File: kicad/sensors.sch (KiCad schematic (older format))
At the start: 13 parts, among them J6 Proximity sensor, U5 KTIR0711S, U7 KTIR0711S, U8 KTIR0711S, U9 KTIR0711S

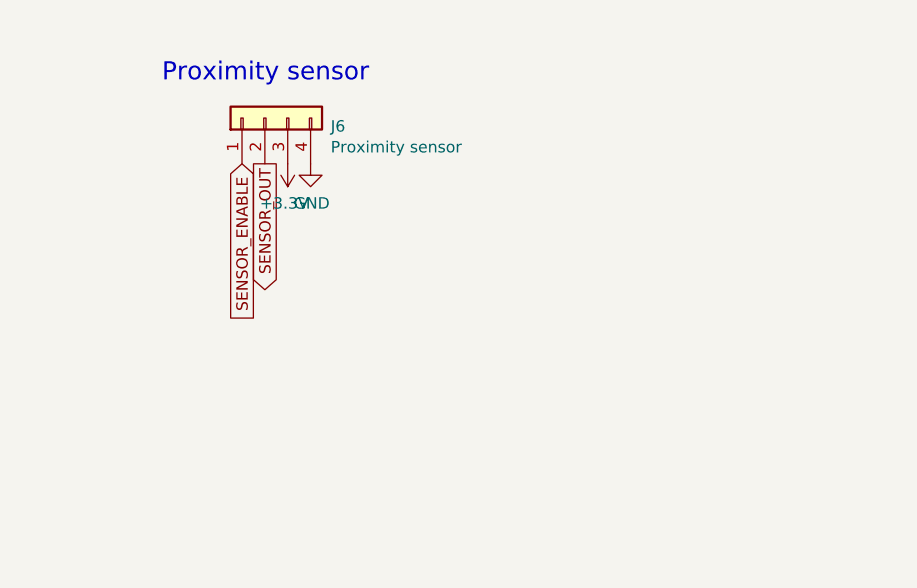
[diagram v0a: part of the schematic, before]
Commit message: fixed diodes, h bridge and modified power supply
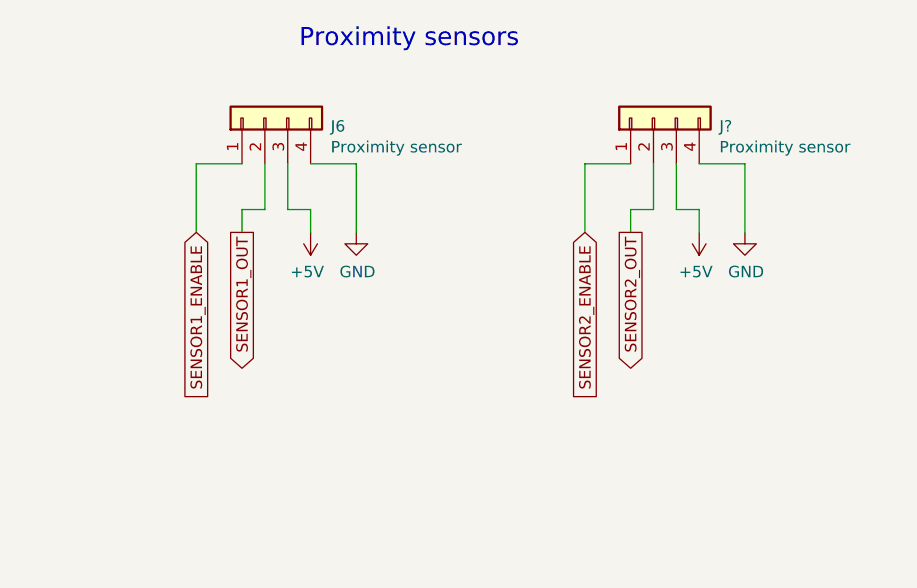
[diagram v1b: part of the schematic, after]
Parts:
- added J?: Proximity sensor, symbol Connector_Generic:Conn_01x04
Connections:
- net +3V3 is gone; now on net +5V: J6.3 (Pin_3)
- net +5V: now also J?.3 (Pin_3)
- net GND: now also J?.4 (Pin_4)
- net SENSOR_ENABLE renamed SENSOR1_ENABLE
- net SENSOR_OUT renamed SENSOR1_OUT
- new net SENSOR2_ENABLE: J?.1 (Pin_1)
- new net SENSOR2_OUT: J?.2 (Pin_2)
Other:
- note added: "Proximity sensors"
- note removed: "Proximity sensor"
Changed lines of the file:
@@
 KTIR_2
-$Comp
-L roboty_mobilne-rescue:KTIR0711S-warsztaty U?
-U 1 1 60BA4003
-P 2150 2350
-AR Path="/60BA4003" Ref="U?"  Part="1"
-AR Path="/60B6A5B0/60BA4003" Ref="U5"  Part="1"
-F 0 "U5" H 2150 2675 50  0000 C CNN
-F 1 "KTIR0711S" H 2150 2584 50  0000 C CNN
-F 2 "" H 1950 2150 50  0000 L CIN
-F 3 "" H 2150 2350 50  0000 L CNN
-	1    2150 2350
-	1    0    0    -1
-$EndComp
 $Comp
 L power:GND #PWR?
@@
 Wire Wire Line
 	1850 2600 2150 2600
-Wire Wire Line
-	2450 2450 2450 2600
-Wire Wire Line
-	2450 2600 2150 2600
-Connection ~ 2150 2600
 $Comp
 L Device:R_Small R?
@@
 	1    0    0    -1
 $EndComp
-$Comp
-L Device:R_Small R?
-U 1 1 60BA401A
-P 2550 2100
-AR Path="/60BA401A" Ref="R?"  Part="1"
-AR Path="/60B6A5B0/60BA401A" Ref="R7"  Part="1"
-F 0 "R7" H 2609 2146 50  0000 L CNN
-F 1 "10k" H 2609 2055 50  0000 L CNN
-F 2 "" V 2480 2100 50  0001 C CNN
-F 3 "~" H 2550 2100 50  0001 C CNN
-	1    2550 2100
-	1    0    0    -1
-$EndComp
 Wire Wire Line
 	1850 2250 1750 2250
-Text GLabel 2700 2250 2    50   Output ~ 0
-KTIR_1
 Text Notes 1650 1600 0    79   ~ 0
 White line sensors
@@
 	1    0    0    -1
 $EndComp
-Connection ~ 2150 1950
-Wire Wire Line
-	2150 1950 2550 1950
 Wire Wire Line
 	1750 3100 2150 3100
@@
 	1750 1950 1750 2000
 Wire Wire Line
-	2450 2250 2550 2250
-Wire Wire Line
 	1750 2200 1750 2250
-Wire Wire Line
-	2550 2200 2550 2250
-Connection ~ 2550 2250
-Wire Wire Line
-	2550 2250 2700 2250
-Wire Wire Line
-	2550 2000 2550 1950
 Wire Wire Line
 	1750 3100 1750 3150
@@
 Wire Wire Line
 	1750 4350 1750 4300
-Text Notes 3900 1600 0    79   ~ 0
-Proximity sensor
+Text Notes 4500 1450 0    79   ~ 0
+Proximity sensors
+$Comp
+L power:+5V #PWR0144
+U 1 1 60AEE18F
+P 2150 3100
+F 0 "#PWR0144" H 2150 2950 50  0001 C CNN
+F 1 "+5V" H 2165 3273 50  0000 C CNN
+F 2 "" H 2150 3100 50  0001 C CNN
+F 3 "" H 2150 3100 50  0001 C CNN
+	1    2150 3100
+	1    0    0    -1
+$EndComp
+Connection ~ 2150 3100
+Wire Wire Line
+	2150 3100 2550 3100
+Connection ~ 2150 1950
+Connection ~ 2150 2600
+Wire Wire Line
+	4050 1950 4050 2250
+Wire Wire Line
+	4250 1950 4050 1950
+Wire Wire Line
+	4750 1950 4750 2250
+Wire Wire Line
+	4550 1950 4750 1950
+$Comp
+L power:+5V #PWR?
+U 1 1 60BD6E0F
+P 4550 2250
+F 0 "#PWR?" H 4550 2100 50  0001 C CNN
+F 1 "+5V" H 4565 2423 50  0000 C CNN
+F 2 "" H 4550 2250 50  0001 C CNN
+F 3 "" H 4550 2250 50  0001 C CNN
+	1    4550 2250
+	-1   0    0    1
+$EndComp
+Text GLabel 4050 2250 3    50   Input ~ 0
+SENSOR1_ENABLE
+Text GLabel 4250 2250 3    50   Output ~ 0
+SENSOR1_OUT
+$Comp
+L power:GND #PWR?
+U 1 1 60BAA02E
+P 4750 2250
+AR Path="/60BAA02E" Ref="#PWR?"  Part="1"
+AR Path="/60B6A5B0/60BAA02E" Ref="#PWR0142"  Part="1"
+F 0 "#PWR0142" H 4750 2000 50  0001 C CNN
+F 1 "GND" H 4755 2077 50  0000 C CNN
+F 2 "" H 4750 2250 50  0001 C CNN
+F 3 "" H 4750 2250 50  0001 C CNN
+	1    4750 2250
+	1    0    0    -1
+$EndComp
 $Comp
 L Connector_Generic:Conn_01x04 J?
@@
 	0    -1   -1   0
 $EndComp
+Wire Wire Line
+	2550 2000 2550 1950
+Wire Wire Line
+	2550 2250 2700 2250
+Connection ~ 2550 2250
+Wire Wire Line
+	2550 2200 2550 2250
+Wire Wire Line
+	2450 2250 2550 2250
+Wire Wire Line
+	2150 1950 2550 1950
+Text GLabel 2700 2250 2    50   Output ~ 0
+KTIR_1
+$Comp
+L Device:R_Small R?
+U 1 1 60BA401A
+P 2550 2100
+AR Path="/60BA401A" Ref="R?"  Part="1"
+AR Path="/60B6A5B0/60BA401A" Ref="R7"  Part="1"
+F 0 "R7" H 2609 2146 50  0000 L CNN
+F 1 "10k" H 2609 2055 50  0000 L CNN
+F 2 "" V 2480 2100 50  0001 C CNN
+F 3 "~" H 2550 2100 50  0001 C CNN
+	1    2550 2100
+	1    0    0    -1
+$EndComp
+Wire Wire Line
+	2450 2600 2150 2600
+Wire Wire Line
+	2450 2450 2450 2600
+$Comp
+L roboty_mobilne-rescue:KTIR0711S-warsztaty U?
+U 1 1 60BA4003
+P 2150 2350
+AR Path="/60BA4003" Ref="U?"  Part="1"
+AR Path="/60B6A5B0/60BA4003" Ref="U5"  Part="1"
+F 0 "U5" H 2150 2675 50  0000 C CNN
+F 1 "KTIR0711S" H 2150 2584 50  0000 C CNN
+F 2 "" H 1950 2150 50  0000 L CIN
+F 3 "" H 2150 2350 50  0000 L CNN
+	1    2150 2350
+	1    0    0    -1
+$EndComp
+Wire Wire Line
+	4250 2250 4250 2150
+Wire Wire Line
+	4250 2150 4350 2150
+Wire Wire Line
+	4350 2150 4350 1950
+Wire Wire Line
+	4550 2250 4550 2150
+Wire Wire Line
+	4550 2150 4450 2150
+Wire Wire Line
+	4450 2150 4450 1950
+Wire Wire Line
+	5750 1950 5750 2250
+Wire Wire Line
+	5950 1950 5750 1950
+Wire Wire Line
+	6450 1950 6450 2250
+Wire Wire Line
+	6250 1950 6450 1950
+$Comp
+L power:+5V #PWR?
+U 1 1 60C05462
+P 6250 2250
+F 0 "#PWR?" H 6250 2100 50  0001 C CNN
+F 1 "+5V" H 6265 2423 50  0000 C CNN
+F 2 "" H 6250 2250 50  0001 C CNN
+F 3 "" H 6250 2250 50  0001 C CNN
+	1    6250 2250
+	-1   0    0    1
+$EndComp
+Text GLabel 5750 2250 3    50   Input ~ 0
+SENSOR2_ENABLE
+Text GLabel 5950 2250 3    50   Output ~ 0
+SENSOR2_OUT
 $Comp
 L power:GND #PWR?
-U 1 1 60BAA02E
-P 4550 1950
-AR Path="/60BAA02E" Ref="#PWR?"  Part="1"
-AR Path="/60B6A5B0/60BAA02E" Ref="#PWR0142"  Part="1"
-F 0 "#PWR0142" H 4550 1700 50  0001 C CNN
-F 1 "GND" H 4555 1777 50  0000 C CNN
-F 2 "" H 4550 1950 50  0001 C CNN
-F 3 "" H 4550 1950 50  0001 C CNN
-	1    4550 1950
-	1    0    0    -1
-$EndComp
-$Comp
-L power:+3.3V #PWR?
-U 1 1 60BAA034
-P 4450 1950
-AR Path="/60BAA034" Ref="#PWR?"  Part="1"
-AR Path="/60B6A5B0/60BAA034" Ref="#PWR0143"  Part="1"
-F 0 "#PWR0143" H 4450 1800 50  0001 C CNN
-F 1 "+3.3V" H 4465 2123 50  0000 C CNN
-F 2 "" H 4450 1950 50  0001 C CNN
-F 3 "" H 4450 1950 50  0001 C CNN
-	1    4450 1950
-	-1   0    0    1
-$EndComp
-Text GLabel 4350 1950 3    50   Output ~ 0
-SENSOR_OUT
-Text GLabel 4250 1950 3    50   Input ~ 0
-SENSOR_ENABLE
-$Comp
-L power:+5V #PWR0144
-U 1 1 60AEE18F
-P 2150 3100
-F 0 "#PWR0144" H 2150 2950 50  0001 C CNN
-F 1 "+5V" H 2165 3273 50  0000 C CNN
-F 2 "" H 2150 3100 50  0001 C CNN
-F 3 "" H 2150 3100 50  0001 C CNN
-	1    2150 3100
-	1    0    0    -1
-$EndComp
-Connection ~ 2150 3100
-Wire Wire Line
-	2150 3100 2550 3100
+U 1 1 60C0546A
+P 6450 2250
+AR Path="/60C0546A" Ref="#PWR?"  Part="1"
+AR Path="/60B6A5B0/60C0546A" Ref="#PWR?"  Part="1"
+F 0 "#PWR?" H 6450 2000 50  0001 C CNN
+F 1 "GND" H 6455 2077 50  0000 C CNN
+F 2 "" H 6450 2250 50  0001 C CNN
+F 3 "" H 6450 2250 50  0001 C CNN
+	1    6450 2250
+	1    0    0    -1
+$EndComp
+$Comp
+L Connector_Generic:Conn_01x04 J?
+U 1 1 60C05470
+P 6050 1750
+AR Path="/60C05470" Ref="J?"  Part="1"
+AR Path="/60B6A5B0/60C05470" Ref="J?"  Part="1"
+F 0 "J?" V 6014 1462 50  0000 R CNN
+F 1 "Proximity sensor" V 5923 1462 50  0000 R CNN
+F 2 "" H 6050 1750 50  0001 C CNN
+F 3 "~" H 6050 1750 50  0001 C CNN
+	1    6050 1750
+	0    -1   -1   0
+$EndComp
+Wire Wire Line
+	5950 2250 5950 2150
+Wire Wire Line
+	5950 2150 6050 2150
+Wire Wire Line
+	6050 2150 6050 1950
+Wire Wire Line
+	6250 2250 6250 2150
+Wire Wire Line
+	6250 2150 6150 2150
+Wire Wire Line
+	6150 2150 6150 1950
 $EndSCHEMATC

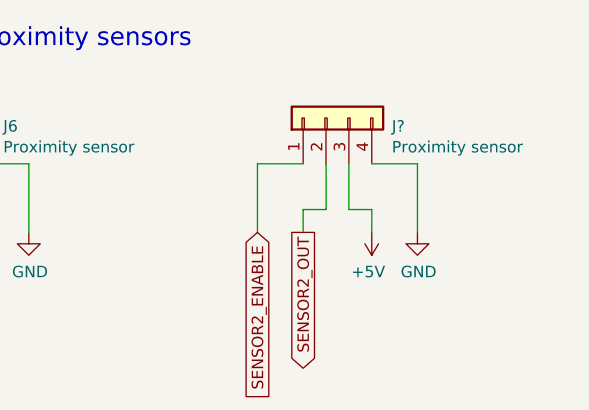
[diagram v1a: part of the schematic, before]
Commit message: deleted 3.3V and modified everything to use 5V instead
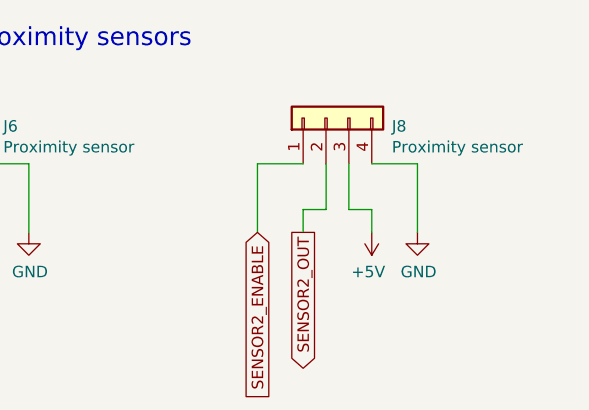
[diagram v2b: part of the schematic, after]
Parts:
- J6: footprint (none) -> Connector_PinSocket_2.54mm:PinSocket_1x04_P2.54mm_Vertical
- J8: renamed from J?; footprint (none) -> Connector_PinSocket_2.54mm:PinSocket_1x04_P2.54mm_Vertical
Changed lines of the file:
@@
 F 0 "U9" H 2150 6225 50  0000 C CNN
 F 1 "KTIR0711S" H 2150 6134 50  0000 C CNN
-F 2 "" H 1950 5700 50  0000 L CIN
+F 2 "" H 1950 5700 50  0001 L CIN
 F 3 "" H 2150 5900 50  0000 L CNN
 	1    2150 5900
@@
 F 0 "U7" H 2150 3825 50  0000 C CNN
 F 1 "KTIR0711S" H 2150 3734 50  0000 C CNN
-F 2 "" H 1950 3300 50  0000 L CIN
+F 2 "" H 1950 3300 50  0001 L CIN
 F 3 "" H 2150 3500 50  0000 L CNN
 	1    2150 3500
@@
 F 0 "U8" H 2150 5025 50  0000 C CNN
 F 1 "KTIR0711S" H 2150 4934 50  0000 C CNN
-F 2 "" H 1950 4500 50  0000 L CIN
+F 2 "" H 1950 4500 50  0001 L CIN
 F 3 "" H 2150 4700 50  0000 L CNN
 	1    2150 4700
@@
 	4550 1950 4750 1950
 $Comp
-L power:+5V #PWR?
+L power:+5V #PWR0145
 U 1 1 60BD6E0F
 P 4550 2250
-F 0 "#PWR?" H 4550 2100 50  0001 C CNN
+F 0 "#PWR0145" H 4550 2100 50  0001 C CNN
 F 1 "+5V" H 4565 2423 50  0000 C CNN
 F 2 "" H 4550 2250 50  0001 C CNN
@@
 F 0 "J6" V 4314 1462 50  0000 R CNN
 F 1 "Proximity sensor" V 4223 1462 50  0000 R CNN
-F 2 "" H 4350 1750 50  0001 C CNN
+F 2 "Connector_PinSocket_2.54mm:PinSocket_1x04_P2.54mm_Vertical" H 4350 1750 50  0001 C CNN
 F 3 "~" H 4350 1750 50  0001 C CNN
 	1    4350 1750
@@
 F 0 "U5" H 2150 2675 50  0000 C CNN
 F 1 "KTIR0711S" H 2150 2584 50  0000 C CNN
-F 2 "" H 1950 2150 50  0000 L CIN
+F 2 "" H 1950 2150 50  0001 L CIN
 F 3 "" H 2150 2350 50  0000 L CNN
 	1    2150 2350
@@
 	6250 1950 6450 1950
 $Comp
-L power:+5V #PWR?
+L power:+5V #PWR0146
 U 1 1 60C05462
 P 6250 2250
-F 0 "#PWR?" H 6250 2100 50  0001 C CNN
+F 0 "#PWR0146" H 6250 2100 50  0001 C CNN
 F 1 "+5V" H 6265 2423 50  0000 C CNN
 F 2 "" H 6250 2250 50  0001 C CNN
@@
 P 6450 2250
 AR Path="/60C0546A" Ref="#PWR?"  Part="1"
-AR Path="/60B6A5B0/60C0546A" Ref="#PWR?"  Part="1"
-F 0 "#PWR?" H 6450 2000 50  0001 C CNN
+AR Path="/60B6A5B0/60C0546A" Ref="#PWR0147"  Part="1"
+F 0 "#PWR0147" H 6450 2000 50  0001 C CNN
 F 1 "GND" H 6455 2077 50  0000 C CNN
 F 2 "" H 6450 2250 50  0001 C CNN
@@
 P 6050 1750
 AR Path="/60C05470" Ref="J?"  Part="1"
-AR Path="/60B6A5B0/60C05470" Ref="J?"  Part="1"
-F 0 "J?" V 6014 1462 50  0000 R CNN
+AR Path="/60B6A5B0/60C05470" Ref="J8"  Part="1"
+F 0 "J8" V 6014 1462 50  0000 R CNN
 F 1 "Proximity sensor" V 5923 1462 50  0000 R CNN
-F 2 "" H 6050 1750 50  0001 C CNN
+F 2 "Connector_PinSocket_2.54mm:PinSocket_1x04_P2.54mm_Vertical" H 6050 1750 50  0001 C CNN
 F 3 "~" H 6050 1750 50  0001 C CNN
 	1    6050 1750

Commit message: created pcb view
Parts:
- R10, R7, R8, R9: footprint (none) -> Resistor_SMD:R_1206_3216Metric_Pad1.30x1.75mm_HandSolder
- R3, R4, R5, R6: value 220 -> 150; footprint (none) -> Resistor_SMD:R_1206_3216Metric_Pad1.30x1.75mm_HandSolder
- U5, U7, U8, U9: footprint (none) -> warsztaty:KTIR0711S
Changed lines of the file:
@@
 F 0 "U9" H 2150 6225 50  0000 C CNN
 F 1 "KTIR0711S" H 2150 6134 50  0000 C CNN
-F 2 "" H 1950 5700 50  0001 L CIN
+F 2 "warsztaty:KTIR0711S" H 1950 5700 50  0001 L CIN
 F 3 "" H 2150 5900 50  0000 L CNN
 	1    2150 5900
@@
 AR Path="/60B6A5B0/60BA3FC5" Ref="R6"  Part="1"
 F 0 "R6" H 1809 5696 50  0000 L CNN
-F 1 "220" H 1809 5605 50  0000 L CNN
-F 2 "" V 1680 5650 50  0001 C CNN
+F 1 "150" H 1809 5605 50  0000 L CNN
+F 2 "Resistor_SMD:R_1206_3216Metric_Pad1.30x1.75mm_HandSolder" V 1680 5650 50  0001 C CNN
 F 3 "~" H 1750 5650 50  0001 C CNN
 	1    1750 5650
@@
 F 0 "R10" H 2609 5696 50  0000 L CNN
 F 1 "10k" H 2609 5605 50  0000 L CNN
-F 2 "" V 2480 5650 50  0001 C CNN
+F 2 "Resistor_SMD:R_1206_3216Metric_Pad1.30x1.75mm_HandSolder" V 2480 5650 50  0001 C CNN
 F 3 "~" H 2550 5650 50  0001 C CNN
 	1    2550 5650
@@
 AR Path="/60B6A5B0/60BA3FD6" Ref="R5"  Part="1"
 F 0 "R5" H 1809 4496 50  0000 L CNN
-F 1 "220" H 1809 4405 50  0000 L CNN
-F 2 "" V 1680 4450 50  0001 C CNN
+F 1 "150" H 1809 4405 50  0000 L CNN
+F 2 "Resistor_SMD:R_1206_3216Metric_Pad1.30x1.75mm_HandSolder" V 1680 4450 50  0001 C CNN
 F 3 "~" H 1750 4450 50  0001 C CNN
 	1    1750 4450
@@
 F 0 "R9" H 2609 4496 50  0000 L CNN
 F 1 "10k" H 2609 4405 50  0000 L CNN
-F 2 "" V 2480 4450 50  0001 C CNN
+F 2 "Resistor_SMD:R_1206_3216Metric_Pad1.30x1.75mm_HandSolder" V 2480 4450 50  0001 C CNN
 F 3 "~" H 2550 4450 50  0001 C CNN
 	1    2550 4450
@@
 F 0 "U7" H 2150 3825 50  0000 C CNN
 F 1 "KTIR0711S" H 2150 3734 50  0000 C CNN
-F 2 "" H 1950 3300 50  0001 L CIN
+F 2 "warsztaty:KTIR0711S" H 1950 3300 50  0001 L CIN
 F 3 "" H 2150 3500 50  0000 L CNN
 	1    2150 3500
@@
 AR Path="/60B6A5B0/60BA3FF5" Ref="R4"  Part="1"
 F 0 "R4" H 1809 3296 50  0000 L CNN
-F 1 "220" H 1809 3205 50  0000 L CNN
-F 2 "" V 1680 3250 50  0001 C CNN
+F 1 "150" H 1809 3205 50  0000 L CNN
+F 2 "Resistor_SMD:R_1206_3216Metric_Pad1.30x1.75mm_HandSolder" V 1680 3250 50  0001 C CNN
 F 3 "~" H 1750 3250 50  0001 C CNN
 	1    1750 3250
@@
 F 0 "R8" H 2609 3296 50  0000 L CNN
 F 1 "10k" H 2609 3205 50  0000 L CNN
-F 2 "" V 2480 3250 50  0001 C CNN
+F 2 "Resistor_SMD:R_1206_3216Metric_Pad1.30x1.75mm_HandSolder" V 2480 3250 50  0001 C CNN
 F 3 "~" H 2550 3250 50  0001 C CNN
 	1    2550 3250
@@
 AR Path="/60B6A5B0/60BA4014" Ref="R3"  Part="1"
 F 0 "R3" H 1809 2146 50  0000 L CNN
-F 1 "220" H 1809 2055 50  0000 L CNN
-F 2 "" V 1680 2100 50  0001 C CNN
+F 1 "150" H 1809 2055 50  0000 L CNN
+F 2 "Resistor_SMD:R_1206_3216Metric_Pad1.30x1.75mm_HandSolder" V 1680 2100 50  0001 C CNN
 F 3 "~" H 1750 2100 50  0001 C CNN
 	1    1750 2100
@@
 F 0 "U8" H 2150 5025 50  0000 C CNN
 F 1 "KTIR0711S" H 2150 4934 50  0000 C CNN
-F 2 "" H 1950 4500 50  0001 L CIN
+F 2 "warsztaty:KTIR0711S" H 1950 4500 50  0001 L CIN
 F 3 "" H 2150 4700 50  0000 L CNN
 	1    2150 4700
@@
 F 0 "R7" H 2609 2146 50  0000 L CNN
 F 1 "10k" H 2609 2055 50  0000 L CNN
-F 2 "" V 2480 2100 50  0001 C CNN
+F 2 "Resistor_SMD:R_1206_3216Metric_Pad1.30x1.75mm_HandSolder" V 2480 2100 50  0001 C CNN
 F 3 "~" H 2550 2100 50  0001 C CNN
 	1    2550 2100
@@
 F 0 "U5" H 2150 2675 50  0000 C CNN
 F 1 "KTIR0711S" H 2150 2584 50  0000 C CNN
-F 2 "" H 1950 2150 50  0001 L CIN
+F 2 "warsztaty:KTIR0711S" H 1950 2150 50  0001 L CIN
 F 3 "" H 2150 2350 50  0000 L CNN
 	1    2150 2350
